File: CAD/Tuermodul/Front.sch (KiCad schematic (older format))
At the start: 44 parts, among them J301 Conn_02x25_Counter_Clockwise, Q301 Q_NPN_CBE, SW301 SW_SPDT_MSM, SW302 SW_SPDT_MSM, SW303 SW_SPDT_MSM, SW304 SW_SPDT_MSM

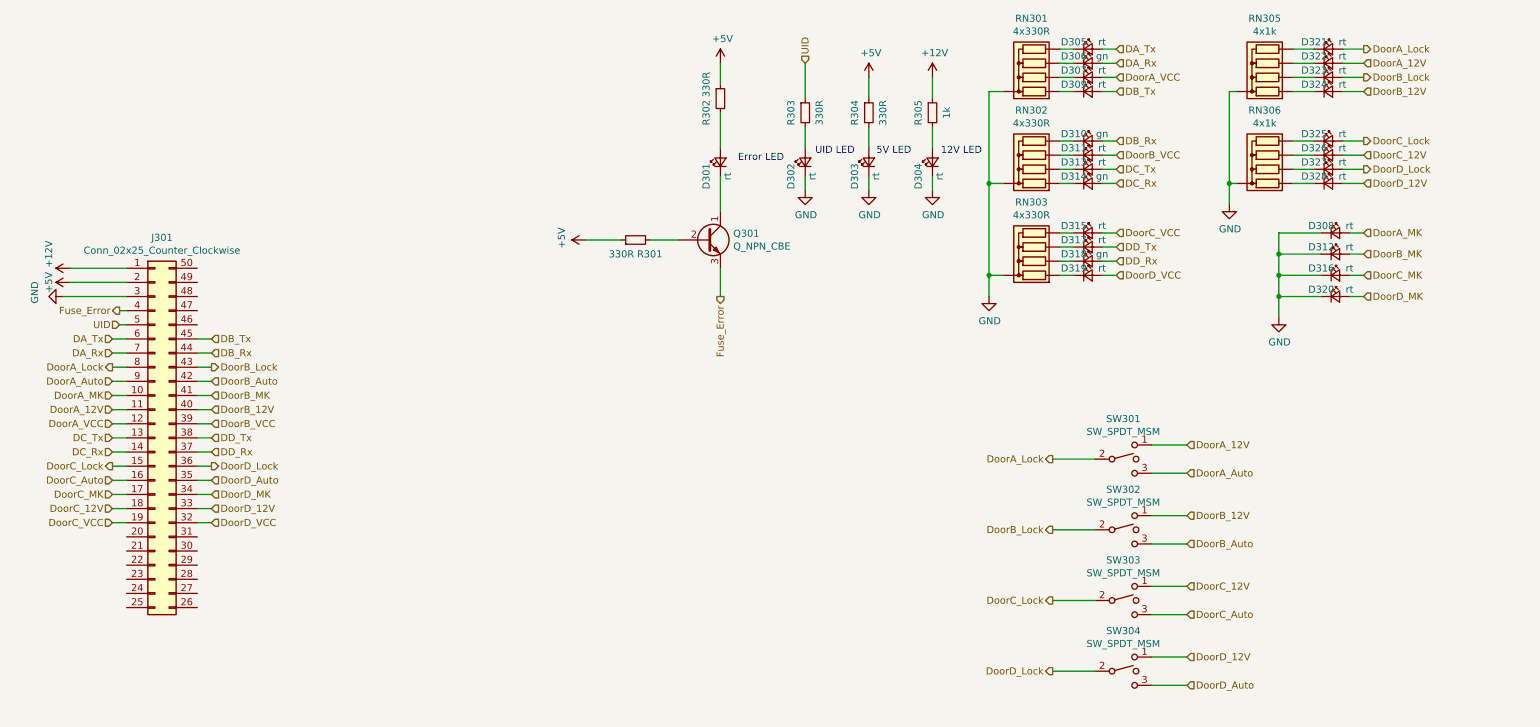
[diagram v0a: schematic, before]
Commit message: -add: switch library for spdt switches -mod: improvements in schematic, bugfixes -mod: placement and routing of the ftdi chip + chicken food
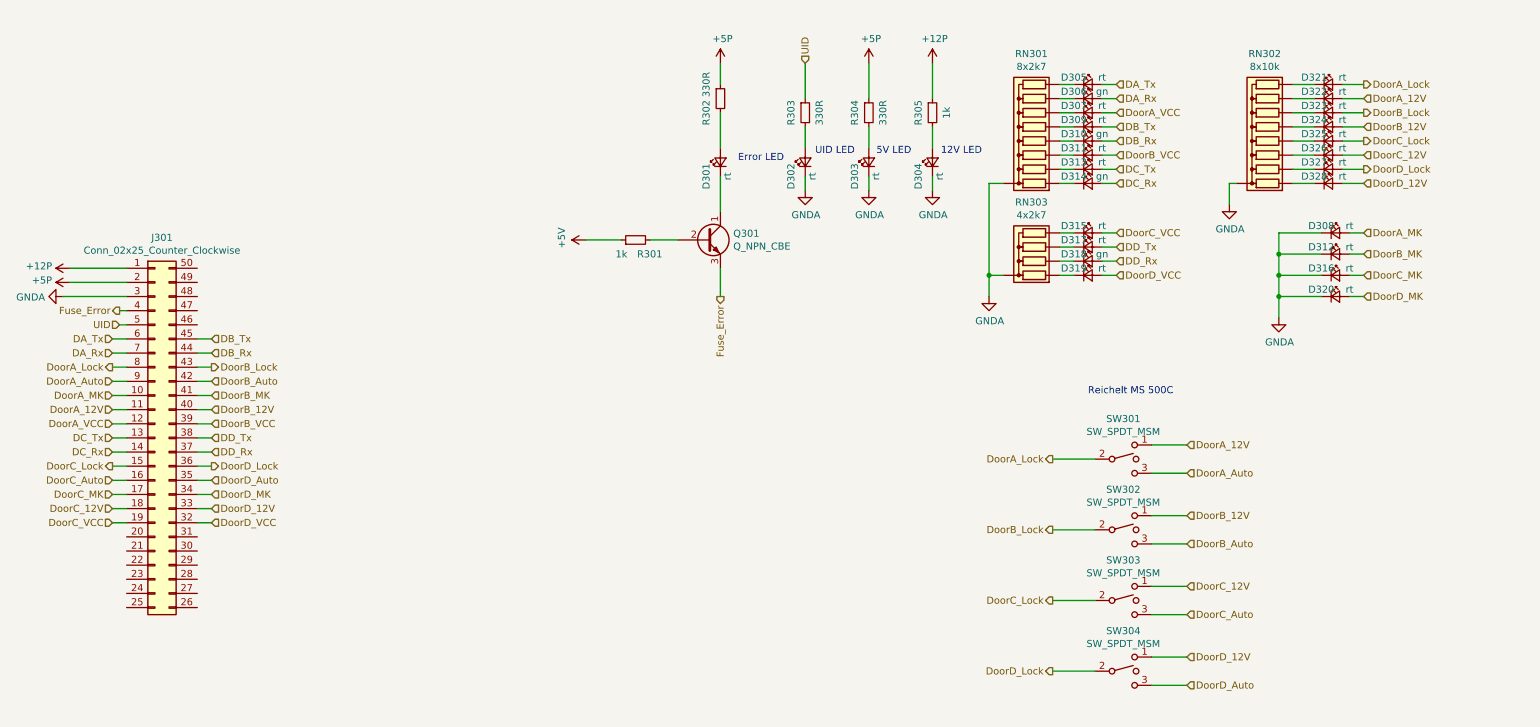
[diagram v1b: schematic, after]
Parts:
- removed RN301, RN302: 4x330R, Resistor_THT:R_Array_SIP5, symbol Device:R_Network04
- removed RN305, RN306: 4x1k, Resistor_THT:R_Array_SIP5, symbol Device:R_Network04
- added RN301: 8x2k7, Resistor_THT:R_Array_SIP9, symbol Device:R_Network08
- added RN302: 8x10k, Resistor_THT:R_Array_SIP9, symbol Device:R_Network08
- R301: value 330R -> 1k
- RN303: value 4x330R -> 4x2k7
- SW301, SW302, SW303, SW304: footprint (none) -> Switches:SPDT
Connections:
- net +5V: no longer J301.2 (Pin_2), R302.1, R304.1
- net at D305.1 (K): now also RN301.9 (R8)
- net at D306.1 (K): now also RN301.8 (R7)
- net at D309.1 (K): now also RN301.6 (R5)
- net at D310.1 (K): now also RN301.5 (R4)
- net at D313.1 (K): now also RN301.3 (R2)
- net at D314.1 (K): now also RN301.2 (R1)
- net at D307.1 (K): now also RN301.7 (R6)
- net at D311.1 (K): now also RN301.4 (R3)
- net at D324.1 (K): now also RN302.6 (R5)
- net at D323.1 (K): now also RN302.7 (R6)
- net at D322.1 (K): now also RN302.8 (R7)
- net at D321.1 (K): now also RN302.9 (R8)
- net at D328.1 (K): now also RN302.2 (R1)
- net at D327.1 (K): now also RN302.3 (R2)
- net at D326.1 (K): now also RN302.4 (R3)
- net at D325.1 (K): now also RN302.5 (R4)
- net +12V renamed +12P
- net GND renamed GNDA
- net GNDA: now also RN301.1 (common), RN302.1 (common)
- new net +5P: J301.2 (Pin_2), R302.1, R304.1
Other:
- note added: "Reichelt MS 500C"
- moved on the sheet: D305, D306, D307, D309, D321, D322, D323, D324

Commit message: -mod: adapted TechSpec due to power enable discussion -mod: changed pin header for front-to-main panel connection -mod: general layout work
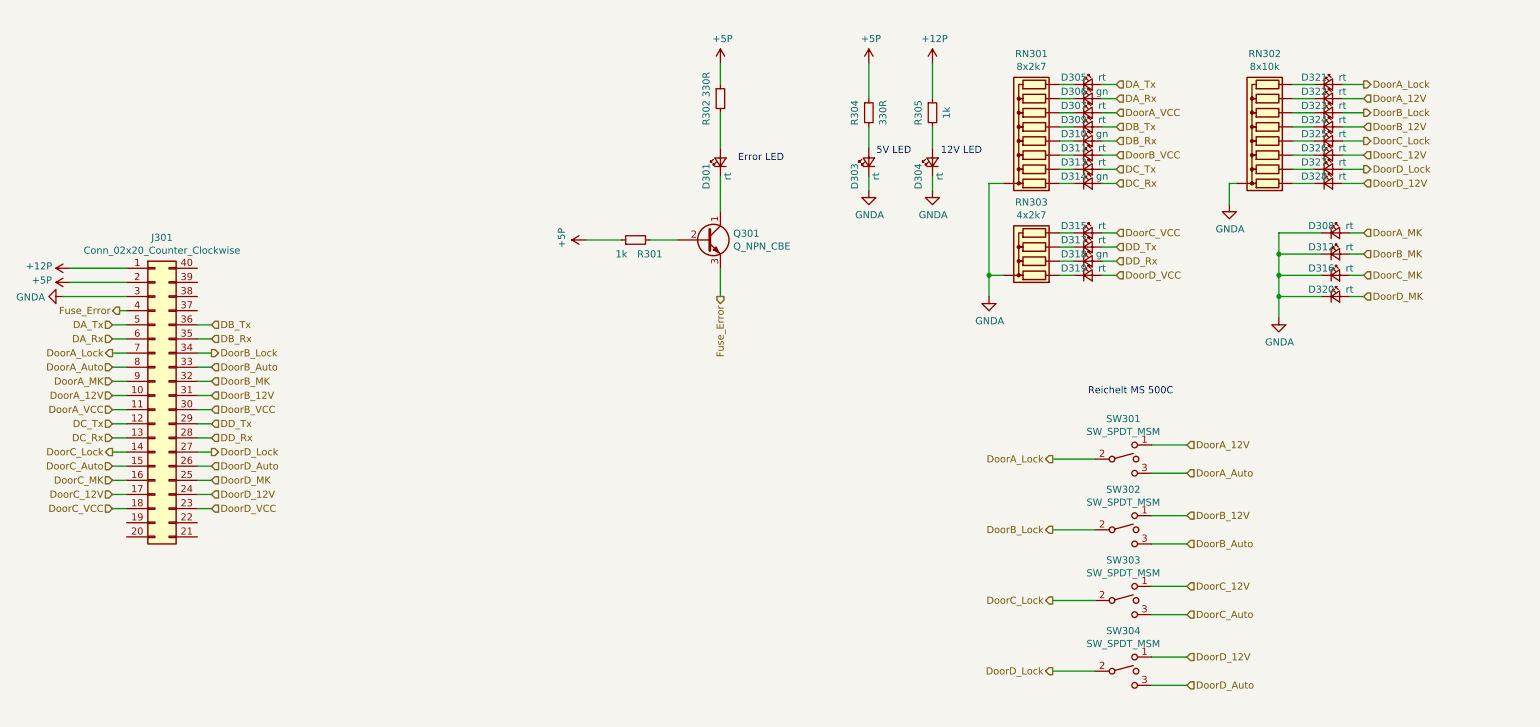
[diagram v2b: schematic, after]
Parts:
- removed D302: rt, LED_THT:LED_D3.0mm, symbol Device:LED_Small
- removed J301: Conn_02x25_Counter_Clockwise, Connector_IDC:IDC-Header_2x25_P2.54mm_Vertical, symbol Connector_Generic:Conn_02x25_Counter_Clockwise
- removed R303: 330R, Resistor_THT:R_Axial_DIN0207_L6.3mm_D2.5mm_P7.62mm_Horizontal, symbol Device:R_Small
- added J301: Conn_02x20_Counter_Clockwise, Connector_PinSocket_2.54mm:PinSocket_2x20_P2.54mm_Vertical_SMD, symbol Connector_Generic:Conn_02x20_Counter_Clockwise
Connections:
- net +5V is gone; now on net +5P: R301.1
- net +12P: now also J301.1 (Pin_1)
- net +5P: now also J301.2 (Pin_2)
- net DA_Rx: now also J301.6 (Pin_6)
- net DA_Tx: now also J301.5 (Pin_5)
- net DB_Rx: now also J301.35 (Pin_35)
- net DB_Tx: now also J301.36 (Pin_36)
- net DC_Rx: now also J301.13 (Pin_13)
- net DC_Tx: now also J301.12 (Pin_12)
- net DD_Rx: now also J301.28 (Pin_28)
- net DD_Tx: now also J301.29 (Pin_29)
- net DoorA_12V: now also J301.10 (Pin_10)
- net DoorA_Auto: now also J301.8 (Pin_8)
- net DoorA_Lock: now also J301.7 (Pin_7)
- net DoorA_MK: now also J301.9 (Pin_9)
- net DoorA_VCC: now also J301.11 (Pin_11)
- net DoorB_12V: now also J301.31 (Pin_31)
- net DoorB_Auto: now also J301.33 (Pin_33)
- net DoorB_Lock: now also J301.34 (Pin_34)
- net DoorB_MK: now also J301.32 (Pin_32)
- net DoorB_VCC: now also J301.30 (Pin_30)
- net DoorC_12V: now also J301.17 (Pin_17)
- net DoorC_Auto: now also J301.15 (Pin_15)
- net DoorC_Lock: now also J301.14 (Pin_14)
- net DoorC_MK: now also J301.16 (Pin_16)
- net DoorC_VCC: now also J301.18 (Pin_18)
- net DoorD_12V: now also J301.24 (Pin_24)
- net DoorD_Auto: now also J301.26 (Pin_26)
- net DoorD_Lock: now also J301.27 (Pin_27)
- net DoorD_MK: now also J301.25 (Pin_25)
- net DoorD_VCC: now also J301.23 (Pin_23)
- net Fuse_Error: now also J301.4 (Pin_4)
- net GNDA: now also J301.3 (Pin_3)
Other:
- note removed: "UID LED"
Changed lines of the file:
@@
 Comment4 ""
 $EndDescr
-Text HLabel 6450 1200 1    50   Input ~ 0
-UID
-$Comp
-L Device:LED_Small D?
-U 1 1 5C5A398D
-P 6450 1900
-AR Path="/5C5A398D" Ref="D?"  Part="1"
-AR Path="/5C5BDAF5/5C5A398D" Ref="D?"  Part="1"
-AR Path="/5C54653F/5C5A398D" Ref="D302"  Part="1"
-F 0 "D302" H 6350 2000 50  0000 C CNN
-F 1 "rt" H 6350 1850 50  0000 C CNN
-F 2 "LED_THT:LED_D3.0mm" V 6450 1900 50  0001 C CNN
-F 3 "~" V 6450 1900 50  0001 C CNN
-	1    6450 1900
-	0    -1   -1   0
-$EndComp
 $Comp
 L Device:Q_NPN_CBE Q?
@@
 Wire Wire Line
 	8550 1350 8650 1350
+Text HLabel 1550 3050 0    50   Input ~ 0
+DA_Tx
 Text HLabel 1550 3150 0    50   Input ~ 0
-DA_Tx
-Text HLabel 1550 3250 0    50   Input ~ 0
 DA_Rx
+Text HLabel 2250 3050 2    50   Input ~ 0
+DB_Tx
 Text HLabel 2250 3150 2    50   Input ~ 0
-DB_Tx
-Text HLabel 2250 3250 2    50   Input ~ 0
 DB_Rx
+Text HLabel 1550 3750 0    50   Input ~ 0
+DC_Tx
 Text HLabel 1550 3850 0    50   Input ~ 0
-DC_Tx
-Text HLabel 1550 3950 0    50   Input ~ 0
 DC_Rx
+Text HLabel 2250 3750 2    50   Input ~ 0
+DD_Tx
 Text HLabel 2250 3850 2    50   Input ~ 0
-DD_Tx
-Text HLabel 2250 3950 2    50   Input ~ 0
 DD_Rx
-$Comp
-L Connector_Generic:Conn_02x25_Counter_Clockwise J?
-U 1 1 5C5A42FA
-P 1850 3850
-AR Path="/5C5BDAF5/5C5A42FA" Ref="J?"  Part="1"
-AR Path="/5C54653F/5C5A42FA" Ref="J301"  Part="1"
-F 0 "J301" H 1900 5267 50  0000 C CNN
-F 1 "Conn_02x25_Counter_Clockwise" H 1900 5176 50  0000 C CNN
-F 2 "Connector_IDC:IDC-Header_2x25_P2.54mm_Vertical" H 1850 3850 50  0001 C CNN
-F 3 "~" H 1850 3850 50  0001 C CNN
-	1    1850 3850
-	1    0    0    -1
-$EndComp
 Wire Wire Line
 	1650 2650 1250 2650
@@
 Wire Wire Line
 	1650 2950 1600 2950
-Text HLabel 1600 3050 0    50   Input ~ 0
-UID
-Wire Wire Line
-	1650 3050 1600 3050
-Text HLabel 1550 3350 0    50   Output ~ 0
+Text HLabel 1550 3250 0    50   Output ~ 0
 DoorA_Lock
+Text HLabel 1550 3450 0    50   Input ~ 0
+DoorA_MK
 Text HLabel 1550 3550 0    50   Input ~ 0
-DoorA_MK
+DoorA_12V
 Text HLabel 1550 3650 0    50   Input ~ 0
-DoorA_12V
-Text HLabel 1550 3750 0    50   Input ~ 0
 DoorA_VCC
-Text HLabel 2250 3350 2    50   Output ~ 0
+Text HLabel 2250 3250 2    50   Output ~ 0
 DoorB_Lock
-Text HLabel 1550 4050 0    50   Output ~ 0
+Text HLabel 1550 3950 0    50   Output ~ 0
 DoorC_Lock
-Text HLabel 2250 4050 2    50   Output ~ 0
+Text HLabel 2250 3950 2    50   Output ~ 0
 DoorD_Lock
+Text HLabel 2250 3450 2    50   Input ~ 0
+DoorB_MK
+Text HLabel 1550 4150 0    50   Input ~ 0
+DoorC_MK
+Text HLabel 2250 4150 2    50   Input ~ 0
+DoorD_MK
 Text HLabel 2250 3550 2    50   Input ~ 0
-DoorB_MK
+DoorB_12V
 Text HLabel 1550 4250 0    50   Input ~ 0
-DoorC_MK
+DoorC_12V
 Text HLabel 2250 4250 2    50   Input ~ 0
-DoorD_MK
+DoorD_12V
 Text HLabel 2250 3650 2    50   Input ~ 0
-DoorB_12V
+DoorB_VCC
 Text HLabel 1550 4350 0    50   Input ~ 0
-DoorC_12V
+DoorC_VCC
 Text HLabel 2250 4350 2    50   Input ~ 0
-DoorD_12V
-Text HLabel 2250 3750 2    50   Input ~ 0
-DoorB_VCC
-Text HLabel 1550 4450 0    50   Input ~ 0
-DoorC_VCC
-Text HLabel 2250 4450 2    50   Input ~ 0
 DoorD_VCC
-Text HLabel 1550 3450 0    50   Input ~ 0
+Text HLabel 1550 3350 0    50   Input ~ 0
 DoorA_Auto
-Text HLabel 2250 3450 2    50   Input ~ 0
+Text HLabel 2250 3350 2    50   Input ~ 0
 DoorB_Auto
-Text HLabel 1550 4150 0    50   Input ~ 0
+Text HLabel 1550 4050 0    50   Input ~ 0
 DoorC_Auto
-Text HLabel 2250 4150 2    50   Input ~ 0
+Text HLabel 2250 4050 2    50   Input ~ 0
 DoorD_Auto
 Wire Wire Line
+	1550 3050 1650 3050
+Wire Wire Line
 	1550 3150 1650 3150
 Wire Wire Line
@@
 	1550 4350 1650 4350
 Wire Wire Line
-	1550 4450 1650 4450
-Wire Wire Line
-	2250 4450 2150 4450
-Wire Wire Line
-	2150 4350 2250 4350
-Wire Wire Line
-	2250 4250 2150 4250
-Wire Wire Line
-	2150 4150 2250 4150
-Wire Wire Line
-	2250 4050 2150 4050
-Wire Wire Line
-	2150 3950 2250 3950
-Wire Wire Line
-	2250 3850 2150 3850
-Wire Wire Line
-	2150 3750 2250 3750
-Wire Wire Line
-	2250 3650 2150 3650
-Wire Wire Line
-	2150 3550 2250 3550
-Wire Wire Line
-	2250 3450 2150 3450
-Wire Wire Line
-	2150 3350 2250 3350
-Wire Wire Line
-	2250 3250 2150 3250
-Wire Wire Line
-	2150 3150 2250 3150
+	2250 4350 2150 4350
+Wire Wire Line
+	2150 4250 2250 4250
+Wire Wire Line
+	2250 4150 2150 4150
+Wire Wire Line
+	2150 4050 2250 4050
+Wire Wire Line
+	2250 3950 2150 3950
+Wire Wire Line
+	2150 3850 2250 3850
+Wire Wire Line
+	2250 3750 2150 3750
+Wire Wire Line
+	2150 3650 2250 3650
+Wire Wire Line
+	2250 3550 2150 3550
+Wire Wire Line
+	2150 3450 2250 3450
+Wire Wire Line
+	2250 3350 2150 3350
+Wire Wire Line
+	2150 3250 2250 3250
+Wire Wire Line
+	2250 3150 2150 3150
+Wire Wire Line
+	2150 3050 2250 3050
 Text HLabel 8650 1350 2    50   Input ~ 0
 DA_Tx
@@
 	0    -1   -1   0
 $EndComp
-$Comp
-L power:+5V #PWR?
-U 1 1 5C6423A6
-P 4900 2450
-AR Path="/5C6423A6" Ref="#PWR?"  Part="1"
-AR Path="/5C5BDAF5/5C6423A6" Ref="#PWR?"  Part="1"
-AR Path="/5C54653F/5C6423A6" Ref="#PWR0304"  Part="1"
-F 0 "#PWR0304" H 4900 2300 50  0001 C CNN
-F 1 "+5V" H 4915 2623 50  0000 C CNN
-F 2 "" H 4900 2450 50  0001 C CNN
-F 3 "" H 4900 2450 50  0001 C CNN
-	1    4900 2450
-	0    -1   -1   0
-$EndComp
-Wire Wire Line
-	6450 2000 6450 2100
-Text Notes 6800 1850 2    50   ~ 0
-UID LED
 Text Notes 7200 1850 2    50   ~ 0
 5V LED
 Wire Wire Line
 	6900 2000 6900 2100
-Wire Wire Line
-	6450 1650 6450 1800
-$Comp
-L Device:R_Small R?
-U 1 1 5C5A3986
-P 6450 1550
-AR Path="/5C5A3986" Ref="R?"  Part="1"
-AR Path="/5C5BDAF5/5C5A3986" Ref="R?"  Part="1"
-AR Path="/5C54653F/5C5A3986" Ref="R303"  Part="1"
-F 0 "R303" V 6350 1550 50  0000 C CNN
-F 1 "330R" V 6550 1550 50  0000 C CNN
-F 2 "Resistor_THT:R_Axial_DIN0207_L6.3mm_D2.5mm_P7.62mm_Horizontal" H 6450 1550 50  0001 C CNN
-F 3 "~" H 6450 1550 50  0001 C CNN
-	1    6450 1550
-	1    0    0    -1
-$EndComp
 Wire Wire Line
 	6900 1650 6900 1800
@@
 Wire Wire Line
 	6900 1200 6900 1450
-Wire Wire Line
-	6450 1200 6450 1450
 Wire Wire Line
 	8250 1350 8350 1350
@@
 $EndComp
 $Comp
-L power:GNDA #PWR0306
-U 1 1 5C5DB722
-P 6450 2100
-F 0 "#PWR0306" H 6450 1850 50  0001 C CNN
-F 1 "GNDA" H 6455 1927 50  0000 C CNN
-F 2 "" H 6450 2100 50  0001 C CNN
-F 3 "" H 6450 2100 50  0001 C CNN
-	1    6450 2100
-	1    0    0    -1
-$EndComp
-$Comp
 L power:GNDA #PWR0308
 U 1 1 5C5DBB47
@@
 	1    0    0    -1
 $EndComp
+$Comp
+L Connector_Generic:Conn_02x20_Counter_Clockwise J?
+U 1 1 5C7AAB1D
+P 1850 3550
+AR Path="/5C5BDAF5/5C7AAB1D" Ref="J?"  Part="1"
+AR Path="/5C54653F/5C7AAB1D" Ref="J301"  Part="1"
+F 0 "J301" H 1900 4667 50  0000 C CNN
+F 1 "Conn_02x20_Counter_Clockwise" H 1900 4576 50  0000 C CNN
+F 2 "Connector_PinSocket_2.54mm:PinSocket_2x20_P2.54mm_Vertical_SMD" H 1850 3550 50  0001 C CNN
+F 3 "~" H 1850 3550 50  0001 C CNN
+	1    1850 3550
+	1    0    0    -1
+$EndComp
+$Comp
+L power:+5P #PWR0144
+U 1 1 5C7BA058
+P 4900 2450
+F 0 "#PWR0144" H 4900 2300 50  0001 C CNN
+F 1 "+5P" H 4915 2623 50  0000 C CNN
+F 2 "" H 4900 2450 50  0001 C CNN
+F 3 "" H 4900 2450 50  0001 C CNN
+	1    4900 2450
+	0    -1   -1   0
+$EndComp
 $EndSCHEMATC

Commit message: -mod: Umbelegung Stecker zwischen Haupt und Frontplatine -add: 100n caps für MK Entprellung -mod: Routing Stecker -mod: Platzierung Front nach Vorgabe
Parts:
- removed RN301: 8x2k7, Resistor_THT:R_Array_SIP9, symbol Device:R_Network08
- removed RN302: 8x10k, Resistor_THT:R_Array_SIP9, symbol Device:R_Network08
- removed RN303: 4x2k7, Resistor_THT:R_Array_SIP5, symbol Device:R_Network04
- added R303: 330R, Resistor_SMD:R_0603_1608Metric_Pad1.05x0.95mm_HandSolder, symbol Device:R_Small
- added R306, R307, R308, R309, R310, R311, R312: 4k7, Resistor_SMD:R_0603_1608Metric_Pad1.05x0.95mm_HandSolder, symbol Device:R_Small
- J301: symbol Connector_Generic:Conn_02x20_Counter_Clockwise -> Connector_Generic:Conn_02x20_Odd_Even
- R301, R302: footprint Resistor_THT:R_Axial_DIN0207_L6.3mm_D2.5mm_P7.62mm_Horizontal -> Resistor_SMD:R_0603_1608Metric_Pad1.05x0.95mm_HandSolder
- R304: value 330R -> 1k; footprint Resistor_THT:R_Axial_DIN0207_L6.3mm_D2.5mm_P7.62mm_Horizontal -> Resistor_SMD:R_0603_1608Metric_Pad1.05x0.95mm_HandSolder
- R305: value 1k -> 4k7; footprint Resistor_THT:R_Axial_DIN0207_L6.3mm_D2.5mm_P7.62mm_Horizontal -> Resistor_SMD:R_0603_1608Metric_Pad1.05x0.95mm_HandSolder
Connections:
- net +12P: now also R304.1; no longer R305.1
- net +5P: now also R303.1; no longer R304.1
- net DA_Rx: now also J301.9 (Pin_9); no longer J301.6 (Pin_6)
- net DA_Tx: now also J301.7 (Pin_7); no longer J301.5 (Pin_5)
- net DB_Rx: now also J301.10 (Pin_10); no longer J301.35 (Pin_35)
- net DB_Tx: now also J301.8 (Pin_8); no longer J301.36 (Pin_36)
- net DC_Rx: now also J301.23 (Pin_23); no longer J301.13 (Pin_13)
- net DC_Tx: now also J301.21 (Pin_21); no longer J301.12 (Pin_12)
- net DD_Rx: now also J301.24 (Pin_24); no longer J301.28 (Pin_28)
- net DD_Tx: now also J301.22 (Pin_22); no longer J301.29 (Pin_29)
- net DoorA_12V: now also J301.13 (Pin_13), R306.2; no longer D322.2 (A), J301.10 (Pin_10)
- net DoorA_Auto: now also J301.17 (Pin_17); no longer J301.8 (Pin_8)
- net DoorA_Lock: now also J301.15 (Pin_15), R305.2; no longer D321.2 (A), J301.7 (Pin_7)
- net DoorA_MK: now also J301.11 (Pin_11); no longer J301.9 (Pin_9)
- net DoorA_VCC: now also J301.5 (Pin_5); no longer J301.11 (Pin_11)
- net DoorB_12V: now also J301.14 (Pin_14), R308.2; no longer D324.2 (A), J301.31 (Pin_31)
- net DoorB_Auto: now also J301.18 (Pin_18); no longer J301.33 (Pin_33)
- net DoorB_Lock: now also J301.16 (Pin_16), R307.2; no longer D323.2 (A), J301.34 (Pin_34)
- net DoorB_MK: now also J301.12 (Pin_12); no longer J301.32 (Pin_32)
- net DoorB_VCC: now also J301.6 (Pin_6); no longer J301.30 (Pin_30)
- net DoorC_12V: now also J301.27 (Pin_27), R310.2; no longer D326.2 (A), J301.17 (Pin_17)
- net DoorC_Auto: now also J301.31 (Pin_31); no longer J301.15 (Pin_15)
- net DoorC_Lock: now also J301.29 (Pin_29), R309.2; no longer D325.2 (A), J301.14 (Pin_14)
- net DoorC_MK: now also J301.25 (Pin_25); no longer J301.16 (Pin_16)
- net DoorC_VCC: now also J301.19 (Pin_19); no longer J301.18 (Pin_18)
- net DoorD_12V: now also J301.28 (Pin_28), R312.2; no longer D328.2 (A), J301.24 (Pin_24)
- net DoorD_Auto: now also J301.32 (Pin_32); no longer J301.26 (Pin_26)
- net DoorD_Lock: now also J301.30 (Pin_30), R311.2; no longer D327.2 (A), J301.27 (Pin_27)
- net DoorD_MK: now also J301.26 (Pin_26); no longer J301.25 (Pin_25)
- net DoorD_VCC: now also J301.20 (Pin_20); no longer J301.23 (Pin_23)
- net Fuse_Error: now also J301.3 (Pin_3); no longer J301.4 (Pin_4)
- net GNDA: now also D305.1 (K), D306.1 (K), D307.1 (K), D309.1 (K), D310.1 (K), D311.1 (K), D313.1 (K), D314.1 (K), D315.1 (K), D317.1 (K), D318.1 (K), D319.1 (K), D321.1 (K), D322.1 (K), D323.1 (K), D324.1 (K), D325.1 (K), D326.1 (K), D327.1 (K), D328.1 (K), J301.33 (Pin_33), J301.34 (Pin_34), J301.35 (Pin_35), J301.36 (Pin_36), J301.37 (Pin_37), J301.38 (Pin_38), J301.39 (Pin_39), J301.4 (Pin_4), J301.40 (Pin_40); no longer J301.3 (Pin_3)
- net at D303.2 (A): now also R303.2; no longer R304.2
- net at D304.2 (A): now also R304.2; no longer R305.2
- new net: D321.2 (A), R305.1
- new net: D322.2 (A), R306.1
- new net: D323.2 (A), R307.1
- new net: D324.2 (A), R308.1
- new net: D325.2 (A), R309.1
- new net: D326.2 (A), R310.1
- new net: D327.2 (A), R311.1
- new net: D328.2 (A), R312.1
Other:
- moved on the sheet: D315, D317, D318, D319
